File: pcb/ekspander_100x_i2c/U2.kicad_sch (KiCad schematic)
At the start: 4 parts, among them J5 DG127A-5.08-06P-14-00AH, J6 DG127A-5.08-06P-14-00AH, J7 DG127A-5.08-06P-14-00AH, U2 MCP23017_SP

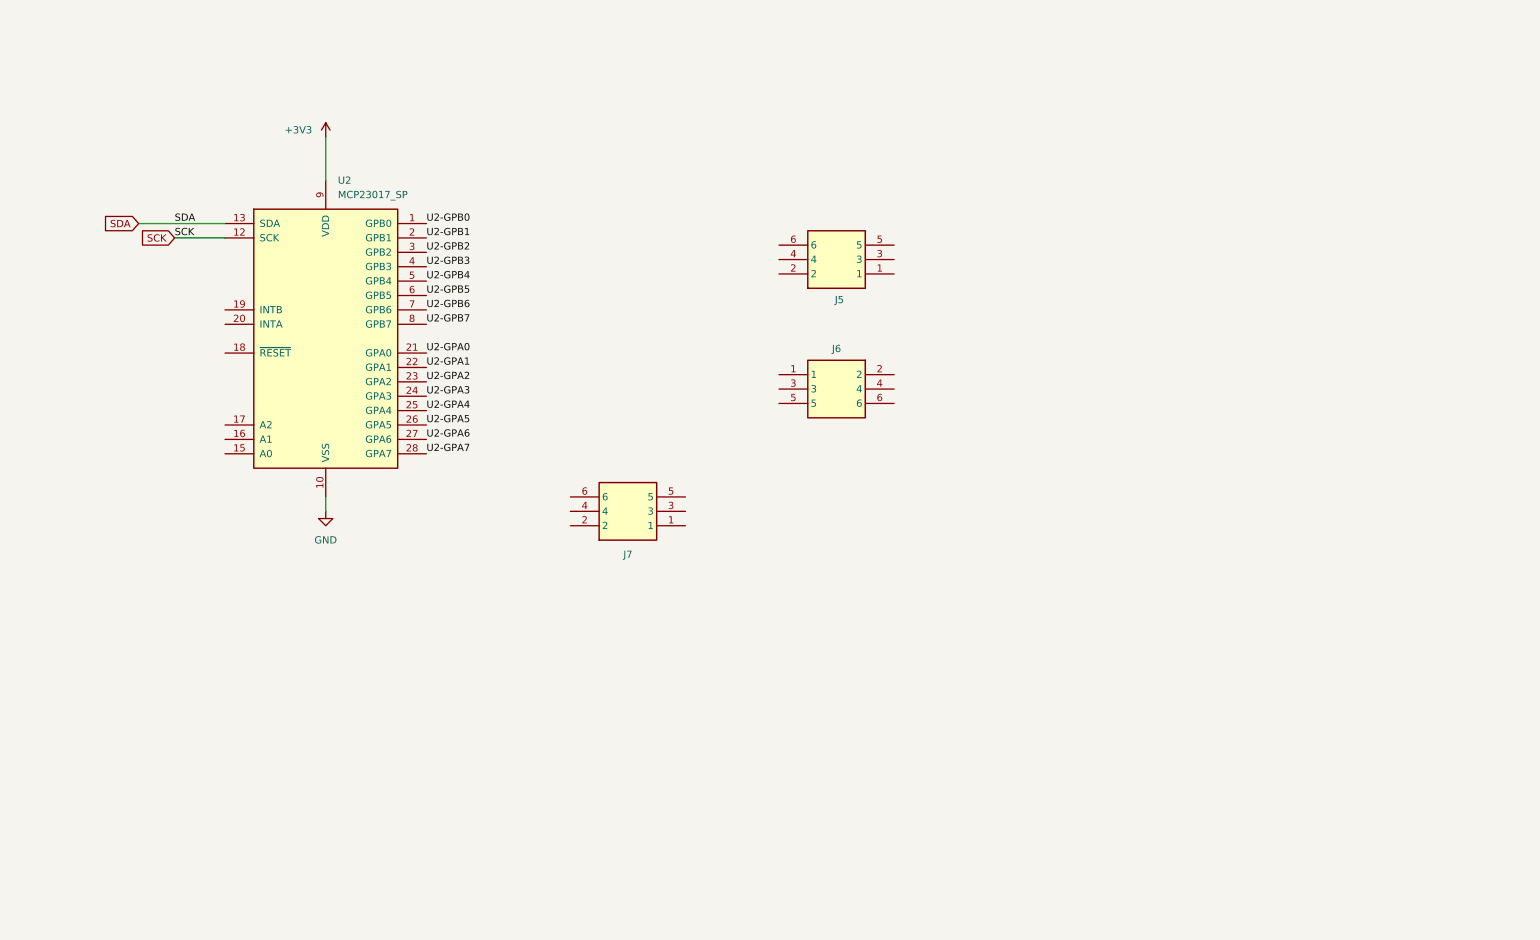
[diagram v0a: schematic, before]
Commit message: Ekspander U2 - U3 - U4 update
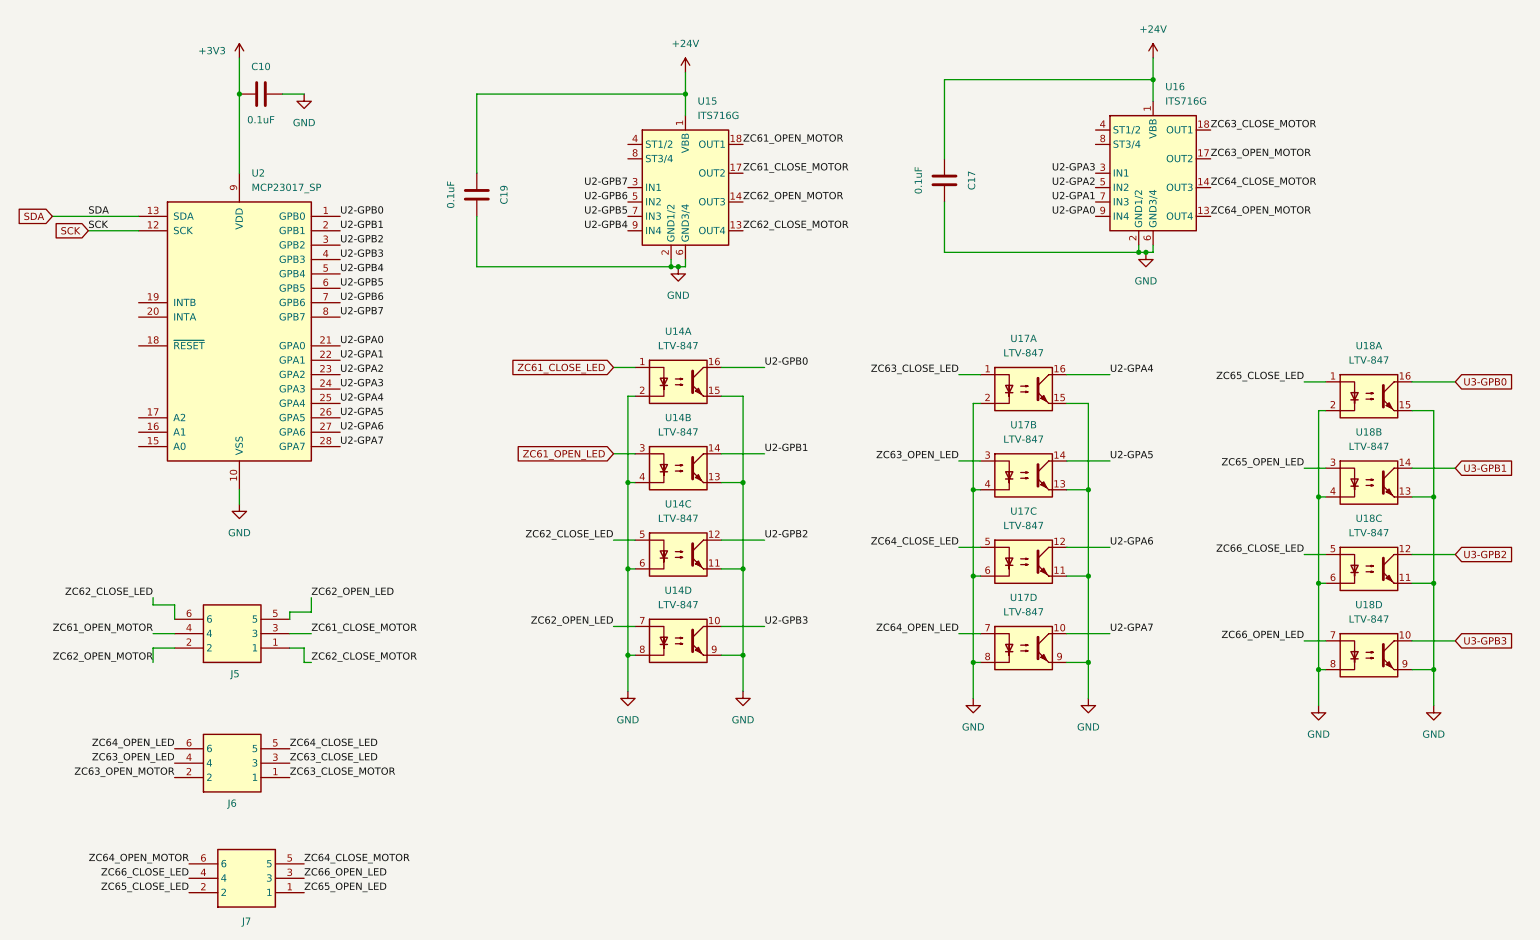
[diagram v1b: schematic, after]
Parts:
- added C10, C17, C19: 0.1uF, Capacitor_SMD:C_0805_2012Metric_Pad1.18x1.45mm_HandSolder, symbol Device:C
- added U14, U17, U18: LTV-847, Package_DIP:DIP-16_W7.62mm, symbol Isolator:LTV-847
- added U15, U16: ITS716G, Package_SO:SOIC-20W_7.5x12.8mm_P1.27mm, symbol Driver_FET:ITS716G
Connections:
- net +3V3: now also C10.1
- net GND: now also C10.2, C17.2, C19.2, U14.11, U14.13, U14.15, U14.2, U14.4, U14.6, U14.8, U14.9, U15.2 (GND1/2), U15.6 (GND3/4), U16.2 (GND1/2), U16.6 (GND3/4), U17.11, U17.13, U17.15, U17.2, U17.4, U17.6, U17.8, U17.9, U18.11, U18.13, U18.15, U18.2, U18.4, U18.6, U18.8, U18.9
- net U2-GPA0: now also U16.9 (IN4)
- net U2-GPA1: now also U16.7 (IN3)
- net U2-GPA2: now also U16.5 (IN2)
- net U2-GPA3: now also U16.3 (IN1)
- net U2-GPA4: now also U17.16
- net U2-GPA5: now also U17.14
- net U2-GPA6: now also U17.12
- net U2-GPA7: now also U17.10
- net U2-GPB0: now also U14.16
- net U2-GPB1: now also U14.14
- net U2-GPB2: now also U14.12
- net U2-GPB3: now also U14.10
- net U2-GPB4: now also U15.9 (IN4)
- net U2-GPB5: now also U15.7 (IN3)
- net U2-GPB6: now also U15.5 (IN2)
- net U2-GPB7: now also U15.3 (IN1)
- net ZC65_OPEN_LED: now reaches J7.1
- net ZC65_OPEN_LED: now also U18.3
- net ZC65_CLOSE_LED: now reaches J7.2
- net ZC65_CLOSE_LED: now also U18.1
- net ZC66_OPEN_LED: now reaches J7.3
- net ZC66_OPEN_LED: now also U18.7
- net ZC66_CLOSE_LED: now reaches J7.4
- net ZC66_CLOSE_LED: now also U18.5
- net ZC64_CLOSE_MOTOR: now reaches J7.5
- net ZC64_CLOSE_MOTOR: now also U16.14 (OUT3)
- net ZC64_OPEN_MOTOR: now reaches J7.6
- net ZC64_OPEN_MOTOR: now also U16.13 (OUT4)
- net ZC63_CLOSE_MOTOR: now reaches J6.1
- net ZC63_CLOSE_MOTOR: now also U16.18 (OUT1)
- net ZC63_OPEN_MOTOR: now reaches J6.2
- net ZC63_OPEN_MOTOR: now also U16.17 (OUT2)
- net ZC63_CLOSE_LED: now reaches J6.3
- net ZC63_CLOSE_LED: now also U17.1
- net ZC63_OPEN_LED: now reaches J6.4
- net ZC63_OPEN_LED: now also U17.3
- net ZC64_CLOSE_LED: now reaches J6.5
- net ZC64_CLOSE_LED: now also U17.5
- net ZC64_OPEN_LED: now reaches J6.6
- net ZC64_OPEN_LED: now also U17.7
- net ZC62_CLOSE_MOTOR: now reaches J5.1
- net ZC62_CLOSE_MOTOR: now also U15.13 (OUT4)
- net ZC62_OPEN_MOTOR: now reaches J5.2
- net ZC62_OPEN_MOTOR: now also U15.14 (OUT3)
- net ZC61_CLOSE_MOTOR: now reaches J5.3
- net ZC61_CLOSE_MOTOR: now also U15.17 (OUT2)
- net ZC61_OPEN_MOTOR: now reaches J5.4
- net ZC61_OPEN_MOTOR: now also U15.18 (OUT1)
- net ZC62_OPEN_LED: now reaches J5.5
- net ZC62_OPEN_LED: now also U14.7
- net ZC62_CLOSE_LED: now reaches J5.6
- net ZC62_CLOSE_LED: now also U14.5
- new net +24V: C17.1, C19.1, U15.1 (VBB), U15.10 (VBB), U15.11 (VBB), U15.12 (VBB), U15.15 (VBB), U15.16 (VBB), U15.19 (VBB), U15.20 (VBB), U16.1 (VBB), U16.10 (VBB), U16.11 (VBB), U16.12 (VBB), U16.15 (VBB), U16.16 (VBB), U16.19 (VBB), U16.20 (VBB)
- new net U3-GPB0: U18.16
- new net U3-GPB1: U18.14
- new net U3-GPB2: U18.12
- new net U3-GPB3: U18.10
- new net ZC61_CLOSE_LED: U14.1
- new net ZC61_OPEN_LED: U14.3
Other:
- moved on the sheet: J5, J6, J7, U2

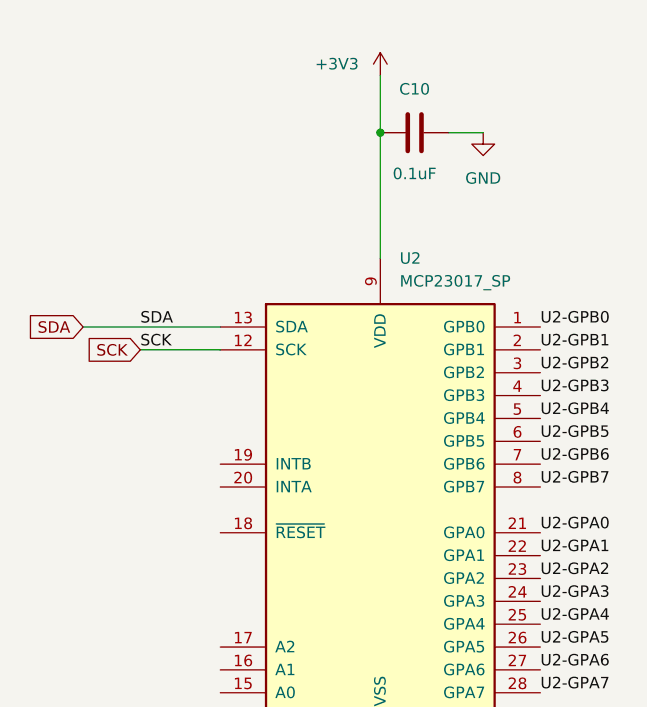
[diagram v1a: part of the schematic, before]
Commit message: Ekspander 24V update
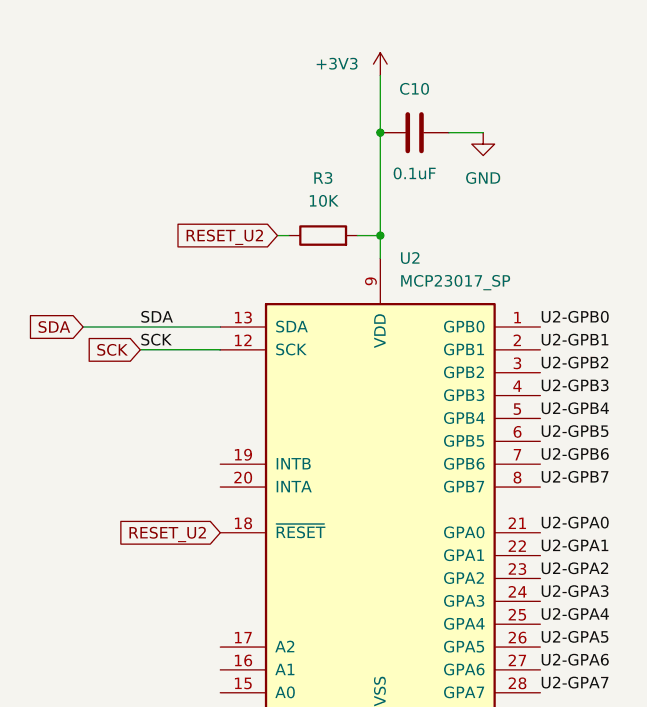
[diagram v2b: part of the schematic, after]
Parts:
- added R3: 10K, PCM_Resistor_SMD_AKL:R_0805_2012Metric_Pad1.20x1.40mm_HandSolder, symbol Device:R
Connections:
- net +3V3: now also R3.2
- net RESET_U2: now reaches U2.18 (~{RESET})
- net RESET_U2: now also R3.1
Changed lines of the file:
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@@
 	)
 	(junction
+		(at 52.07 35.56)
+		(diameter 0)
+		(color 0 0 0 0)
+	)
+	(junction
 		(at 201.93 109.22)
 		(diameter 0)
@@
 	(wire
 		(pts
+			(xy 40.64 35.56) (xy 41.91 35.56)
+		)
+		(stroke
+			(width 0)
+			(type default)
+		)
+	)
+	(wire
+		(pts
 			(xy 266.7 105.41) (xy 259.08 105.41)
 		)
@@
 	(wire
 		(pts
+			(xy 49.53 35.56) (xy 52.07 35.56)
+		)
+		(stroke
+			(width 0)
+			(type default)
+		)
+	)
+	(wire
+		(pts
 			(xy 181.61 124.46) (xy 181.61 130.81)
 		)
@@
 	(wire
 		(pts
-			(xy 52.07 24.13) (xy 52.07 38.1)
+			(xy 52.07 24.13) (xy 52.07 35.56)
 		)
 		(stroke
@@
 	(wire
 		(pts
+			(xy 52.07 35.56) (xy 52.07 38.1)
+		)
+		(stroke
+			(width 0)
+			(type default)
+		)
+	)
+	(wire
+		(pts
 			(xy 262.89 110.49) (xy 262.89 125.73)
 		)
@@
 		)
 	)
+	(global_label "RESET_U2"
+		(shape input)
+		(at 34.29 68.58 180)
+		(fields_autoplaced yes)
+		(effects
+			(font
+				(size 1.27 1.27)
+			)
+			(justify right)
+		)
+		(property "Intersheetrefs" "${INTERSHEET_REFS}"
+			(at 22.0521 68.58 0)
+			(effects
+				(font
+					(size 1.27 1.27)
+				)
+				(justify right)
+				(hide yes)
+			)
+		)
+	)
 	(global_label "U3-GPB1"
 		(shape input)
@@
 		)
 	)
+	(global_label "RESET_U2"
+		(shape input)
+		(at 40.64 35.56 180)
+		(fields_autoplaced yes)
+		(effects
+			(font
+				(size 1.27 1.27)
+			)
+			(justify right)
+		)
+		(property "Intersheetrefs" "${INTERSHEET_REFS}"
+			(at 28.4021 35.56 0)
+			(effects
+				(font
+					(size 1.27 1.27)
+				)
+				(justify right)
+				(hide yes)
+			)
+		)
+	)
 	(global_label "SDA"
 		(shape input)
@@
 					(unit 1)
 				)
+			)
+		)
+	)
+	(symbol
+		(lib_id "Device:R")
+		(at 45.72 35.56 90)
+		(unit 1)
+		(exclude_from_sim no)
+		(in_bom yes)
+		(on_board yes)
+		(dnp no)
+		(fields_autoplaced yes)
+		(property "Reference" "R3"
+			(at 45.72 29.21 90)
+			(effects
+				(font
+					(size 1.27 1.27)
+				)
+			)
+		)
+		(property "Value" "10K"
+			(at 45.72 31.75 90)
+			(effects
+				(font
+					(size 1.27 1.27)
+				)
+			)
+		)
+		(property "Footprint" "PCM_Resistor_SMD_AKL:R_0805_2012Metric_Pad1.20x1.40mm_HandSolder"
+			(at 45.72 37.338 90)
+			(effects
+				(font
+					(size 1.27 1.27)
+				)
+				(hide yes)
+			)
+		)
+		(property "Datasheet" "~"
+			(at 45.72 35.56 0)
+			(effects
+				(font
+					(size 1.27 1.27)
+				)
+				(hide yes)
+			)
+		)
+		(property "Description" "Resistor"
+			(at 45.72 35.56 0)
+			(effects
+				(font
+					(size 1.27 1.27)
+				)
+				(hide yes)
+			)
+		)
+		(pin "2"
+		)
+		(pin "1"
+		)
+		(instances
+			(project "ekspander_100x_i2c"
+				(path "/824ceec5-564f-405b-8bea-e5a9f7aa2926/24a537b1-e78d-4d9d-9041-2847cfe4bae7"
+					(reference "R3")
+					(unit 1)
+				)

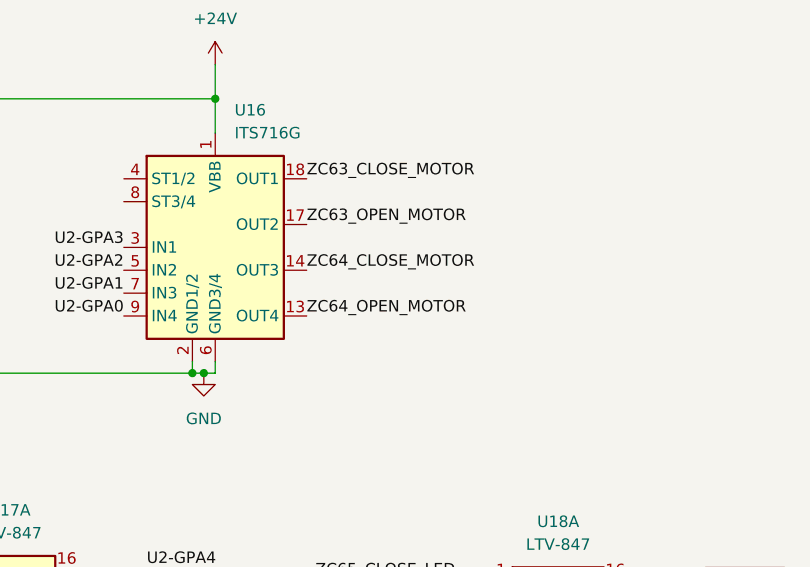
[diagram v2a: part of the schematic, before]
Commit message: Ekspander 100x - PCB layout V2
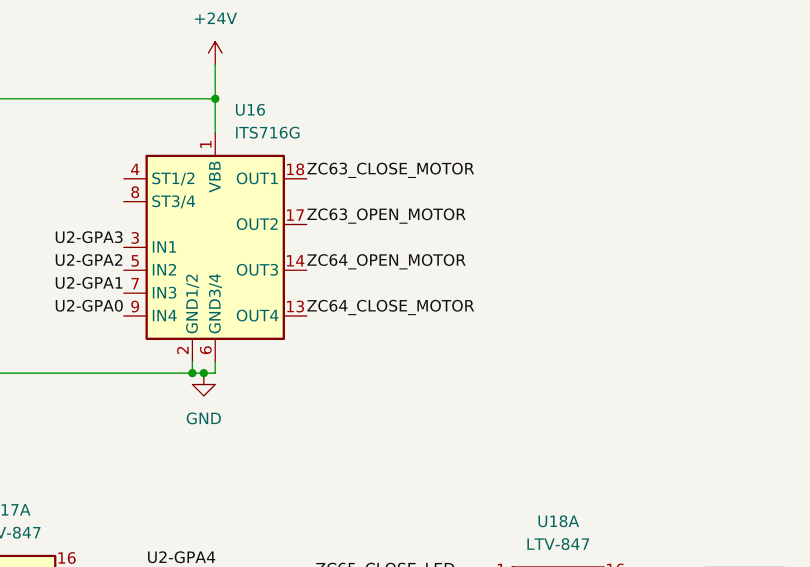
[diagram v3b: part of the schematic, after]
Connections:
- net ZC64_CLOSE_MOTOR: now also U16.13 (OUT4); no longer U16.14 (OUT3)
- net ZC64_OPEN_MOTOR: now also U16.14 (OUT3); no longer U16.13 (OUT4)
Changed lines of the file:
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@@
 	)
 	(label "ZC64_OPEN_MOTOR"
-		(at 223.52 45.72 0)
-		(fields_autoplaced yes)
-		(effects
-			(font
-				(size 1.27 1.27)
-			)
-			(justify left bottom)
-		)
-		(property "Netclass" "+24V"
-			(at 223.52 46.99 0)
+		(at 223.52 40.64 0)
+		(fields_autoplaced yes)
+		(effects
+			(font
+				(size 1.27 1.27)
+			)
+			(justify left bottom)
+		)
+		(property "Netclass" "+24V"
+			(at 223.52 41.91 0)
 			(effects
 				(font
@@
 	)
 	(label "ZC64_CLOSE_MOTOR"
-		(at 223.52 40.64 0)
-		(fields_autoplaced yes)
-		(effects
-			(font
-				(size 1.27 1.27)
-			)
-			(justify left bottom)
-		)
-		(property "Netclass" "+24V"
-			(at 223.52 41.91 0)
-			(effects
-				(font
+		(at 223.52 45.72 0)
+		(fields_autoplaced yes)
+		(effects
+			(font
+				(size 1.27 1.27)
+			)
+			(justify left bottom)
+		)
+		(property "Netclass" "+24V"
+			(at 223.52 46.99 0)
+			(effects
+				(font
